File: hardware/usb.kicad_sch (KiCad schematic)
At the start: 2 parts

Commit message: Add the Cube project
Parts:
- added C?: 100n, Capacitor_SMD:C_0402_1005Metric_Pad0.74x0.62mm_HandSolder, symbol Device:C_Small
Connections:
- net +5V: now also C?.1
- net GND: now also C?.2
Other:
- note removed: "Place close to the connector"
- moved on the sheet: J?, U?

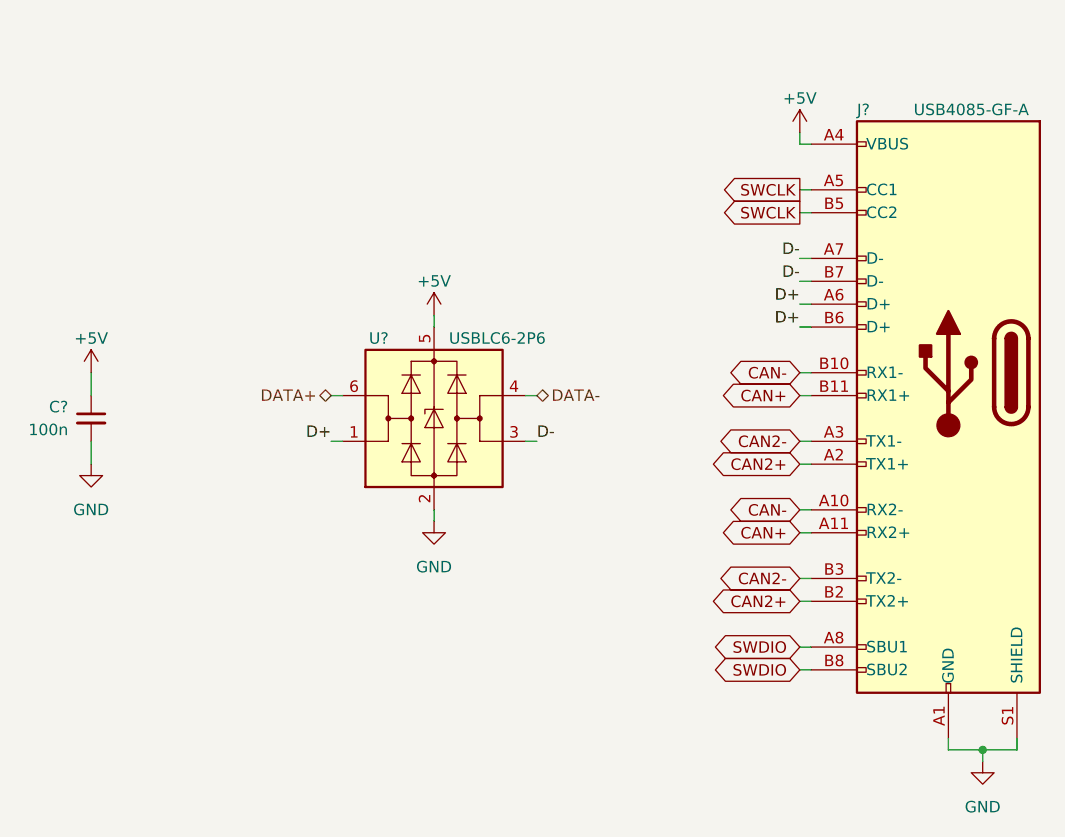
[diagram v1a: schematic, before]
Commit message: Improve the schematic
- add anti-aliasing filters
- rearrange the main connector signals
- improve the power filtering
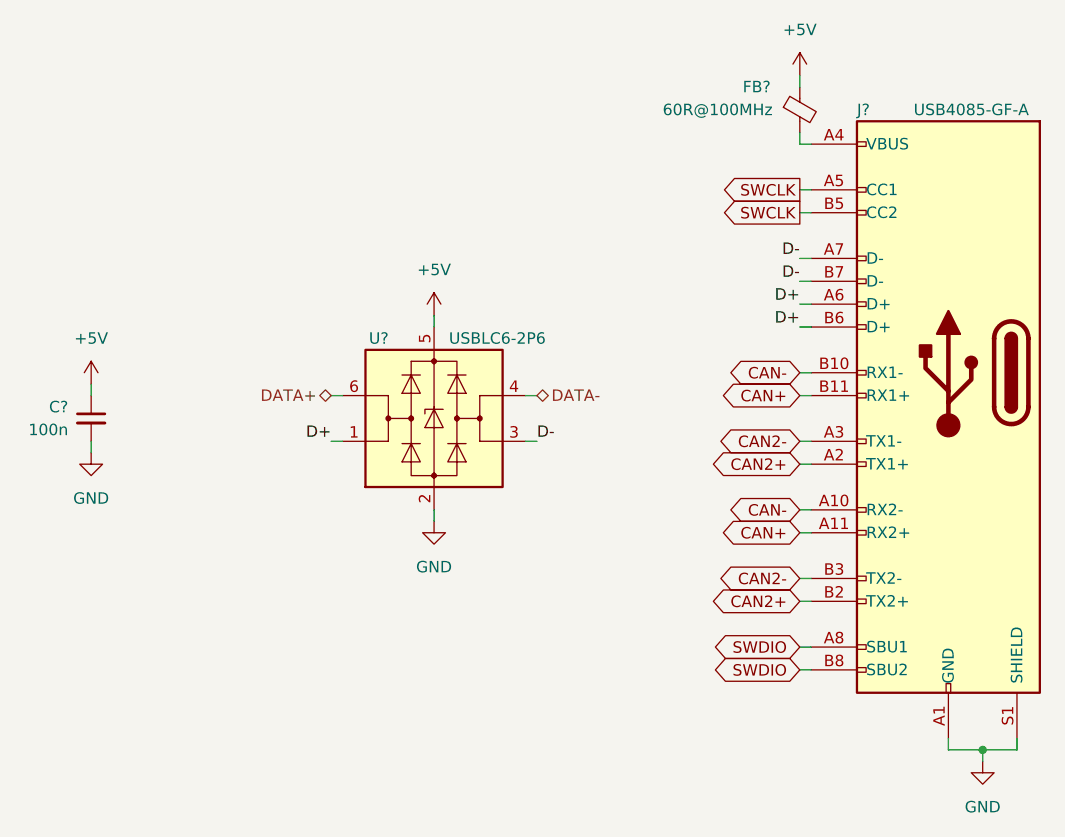
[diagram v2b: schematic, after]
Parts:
- added FB?: 60R@100MHz, Inductor_SMD:L_0603_1608Metric, symbol Device:FerriteBead_Small
- C?: footprint Capacitor_SMD:C_0402_1005Metric_Pad0.74x0.62mm_HandSolder -> Capacitor_SMD:C_0603_1608Metric
- J?: footprint Frontbox:CUI_UJ31-CH-31-SMT-TR -> Local_Library:CUI_UJ31-CH-31-SMT-TR
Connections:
- net +5V: now also FB?.1; no longer J?.A4 (VBUS), J?.A9 (VBUS), J?.B4 (VBUS), J?.B9 (VBUS)
- new net: FB?.2, J?.A4 (VBUS), J?.A9 (VBUS), J?.B4 (VBUS), J?.B9 (VBUS)
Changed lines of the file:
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@@
     (stroke (width 0) (type default))
   )
-  (wire (pts (xy 101.6 101.6) (xy 101.6 104.14))
+  (wire (pts (xy 101.6 101.6) (xy 101.6 102.87))
     (stroke (width 0) (type default))
   )
@@
     (stroke (width 0) (type default))
   )
-  (wire (pts (xy 101.6 93.98) (xy 101.6 96.52))
+  (wire (pts (xy 101.6 95.25) (xy 101.6 96.52))
+    (stroke (width 0) (type default))
+  )
+  (wire (pts (xy 180.34 60.96) (xy 180.34 62.23))
     (stroke (width 0) (type default))
   )
@@
     (effects (font (size 1.27 1.27)) (justify left))
   )
-  (symbol (lib_id "power:GND") (at 101.6 104.14 0) (unit 1)
-    (in_bom yes) (on_board yes) (dnp no)
-    (property "Reference" "#PWR?" (at 101.6 110.49 0)
-      (effects (font (size 1.27 1.27)) hide)
-    )
-    (property "Value" "GND" (at 101.6 109.22 0)
-      (effects (font (size 1.27 1.27)))
-    )
-    (property "Footprint" "" (at 101.6 104.14 0)
-      (effects (font (size 1.27 1.27)) hide)
-    )
-    (property "Datasheet" "" (at 101.6 104.14 0)
-      (effects (font (size 1.27 1.27)) hide)
-    )
-    (pin "1")
-    (instances
-      (project "rearbox"
-        (path "/b652b05a-4e3d-4ad1-b032-18886abe7d45"
-          (reference "#PWR?") (unit 1)
-        )
-        (path "/b652b05a-4e3d-4ad1-b032-18886abe7d45/1a71c66a-e6f2-4e7d-92f3-10826884049d"
-          (reference "#PWR0107") (unit 1)
-        )
-      )
-    )
-  )
-  (symbol (lib_id "power:+5V") (at 180.34 67.31 0) (mirror y) (unit 1)
-    (in_bom yes) (on_board yes) (dnp no) (fields_autoplaced)
-    (property "Reference" "#PWR?" (at 180.34 71.12 0)
-      (effects (font (size 1.27 1.27)) hide)
-    )
-    (property "Value" "+5V" (at 180.34 63.5 0)
-      (effects (font (size 1.27 1.27)))
-    )
-    (property "Footprint" "" (at 180.34 67.31 0)
-      (effects (font (size 1.27 1.27)) hide)
-    )
-    (property "Datasheet" "" (at 180.34 67.31 0)
+  (symbol (lib_id "power:GND") (at 101.6 102.87 0) (unit 1)
+    (in_bom yes) (on_board yes) (dnp no)
+    (property "Reference" "#PWR?" (at 101.6 109.22 0)
+      (effects (font (size 1.27 1.27)) hide)
+    )
+    (property "Value" "GND" (at 101.6 107.95 0)
+      (effects (font (size 1.27 1.27)))
+    )
+    (property "Footprint" "" (at 101.6 102.87 0)
+      (effects (font (size 1.27 1.27)) hide)
+    )
+    (property "Datasheet" "" (at 101.6 102.87 0)
+      (effects (font (size 1.27 1.27)) hide)
+    )
+    (pin "1")
+    (instances
+      (project "rearbox"
+        (path "/b652b05a-4e3d-4ad1-b032-18886abe7d45"
+          (reference "#PWR?") (unit 1)
+        )
+        (path "/b652b05a-4e3d-4ad1-b032-18886abe7d45/1a71c66a-e6f2-4e7d-92f3-10826884049d"
+          (reference "#PWR0121") (unit 1)
+        )
+      )
+    )
+  )
+  (symbol (lib_id "power:+5V") (at 180.34 60.96 0) (mirror y) (unit 1)
+    (in_bom yes) (on_board yes) (dnp no)
+    (property "Reference" "#PWR?" (at 180.34 64.77 0)
+      (effects (font (size 1.27 1.27)) hide)
+    )
+    (property "Value" "+5V" (at 180.34 55.88 0)
+      (effects (font (size 1.27 1.27)))
+    )
+    (property "Footprint" "" (at 180.34 60.96 0)
+      (effects (font (size 1.27 1.27)) hide)
+    )
+    (property "Datasheet" "" (at 180.34 60.96 0)
       (effects (font (size 1.27 1.27)) hide)
     )
@@
         )
         (path "/b652b05a-4e3d-4ad1-b032-18886abe7d45/1a71c66a-e6f2-4e7d-92f3-10826884049d"
-          (reference "#PWR0110") (unit 1)
+          (reference "#PWR0124") (unit 1)
+        )
+      )
+    )
+  )
+  (symbol (lib_id "Device:FerriteBead_Small") (at 180.34 64.77 0) (unit 1)
+    (in_bom yes) (on_board yes) (dnp no)
+    (property "Reference" "FB?" (at 173.99 62.23 0)
+      (effects (font (size 1.27 1.27)) (justify left))
+    )
+    (property "Value" "60R@100MHz" (at 165.1 64.77 0)
+      (effects (font (size 1.27 1.27)) (justify left))
+    )
+    (property "Footprint" "Inductor_SMD:L_0603_1608Metric" (at 178.562 64.77 90)
+      (effects (font (size 1.27 1.27)) hide)
+    )
+    (property "Datasheet" "~" (at 180.34 64.77 0)
+      (effects (font (size 1.27 1.27)) hide)
+    )
+    (pin "1")
+    (pin "2")
+    (instances
+      (project "rearbox"
+        (path "/b652b05a-4e3d-4ad1-b032-18886abe7d45/38408e41-dfb1-4c27-acb0-3f1224cc8789"
+          (reference "FB?") (unit 1)
+        )
+        (path "/b652b05a-4e3d-4ad1-b032-18886abe7d45/38408e41-dfb1-4c27-acb0-3f1224cc8789/eec2c93a-0fce-4d3a-ab43-9e1e0481c06c"
+          (reference "FB3") (unit 1)
+        )
+        (path "/b652b05a-4e3d-4ad1-b032-18886abe7d45/38408e41-dfb1-4c27-acb0-3f1224cc8789/f1ed15a3-9302-436f-b25a-713477aeadf3"
+          (reference "FB1") (unit 1)
+        )
+        (path "/b652b05a-4e3d-4ad1-b032-18886abe7d45/1a71c66a-e6f2-4e7d-92f3-10826884049d"
+          (reference "FB7") (unit 1)
         )
       )
@@
         )
         (path "/b652b05a-4e3d-4ad1-b032-18886abe7d45/1a71c66a-e6f2-4e7d-92f3-10826884049d"
-          (reference "U12") (unit 1)
-        )
-      )
-    )
-  )
-  (symbol (lib_id "power:+5V") (at 101.6 93.98 0) (unit 1)
-    (in_bom yes) (on_board yes) (dnp no) (fields_autoplaced)
-    (property "Reference" "#PWR?" (at 101.6 97.79 0)
+          (reference "U13") (unit 1)
+        )
+      )
+    )
+  )
+  (symbol (lib_id "power:+5V") (at 101.6 95.25 0) (unit 1)
+    (in_bom yes) (on_board yes) (dnp no)
+    (property "Reference" "#PWR?" (at 101.6 99.06 0)
       (effects (font (size 1.27 1.27)) hide)
     )
@@
       (effects (font (size 1.27 1.27)))
     )
-    (property "Footprint" "" (at 101.6 93.98 0)
-      (effects (font (size 1.27 1.27)) hide)
-    )
-    (property "Datasheet" "" (at 101.6 93.98 0)
-      (effects (font (size 1.27 1.27)) hide)
-    )
-    (pin "1")
-    (instances
-      (project "rearbox"
-        (path "/b652b05a-4e3d-4ad1-b032-18886abe7d45"
-          (reference "#PWR?") (unit 1)
-        )
-        (path "/b652b05a-4e3d-4ad1-b032-18886abe7d45/1a71c66a-e6f2-4e7d-92f3-10826884049d"
-          (reference "#PWR0106") (unit 1)
+    (property "Footprint" "" (at 101.6 95.25 0)
+      (effects (font (size 1.27 1.27)) hide)
+    )
+    (property "Datasheet" "" (at 101.6 95.25 0)
+      (effects (font (size 1.27 1.27)) hide)
+    )
+    (pin "1")
+    (instances
+      (project "rearbox"
+        (path "/b652b05a-4e3d-4ad1-b032-18886abe7d45"
+          (reference "#PWR?") (unit 1)
+        )
+        (path "/b652b05a-4e3d-4ad1-b032-18886abe7d45/1a71c66a-e6f2-4e7d-92f3-10826884049d"
+          (reference "#PWR0120") (unit 1)
         )
       )
@@
         )
         (path "/b652b05a-4e3d-4ad1-b032-18886abe7d45/1a71c66a-e6f2-4e7d-92f3-10826884049d"
-          (reference "#PWR0109") (unit 1)
+          (reference "#PWR0123") (unit 1)
         )
       )
@@
       (effects (font (size 1.27 1.27)))
     )
-    (property "Footprint" "Frontbox:CUI_UJ31-CH-31-SMT-TR" (at 193.04 93.98 0)
+    (property "Footprint" "Local_Library:CUI_UJ31-CH-31-SMT-TR" (at 193.04 93.98 0)
       (effects (font (size 1.27 1.27)) hide)
     )
@@
   )
   (symbol (lib_id "power:+5V") (at 139.7 87.63 0) (unit 1)
-    (in_bom yes) (on_board yes) (dnp no) (fields_autoplaced)
+    (in_bom yes) (on_board yes) (dnp no)
     (property "Reference" "#PWR?" (at 139.7 91.44 0)
       (effects (font (size 1.27 1.27)) hide)
     )
-    (property "Value" "+5V" (at 139.7 83.82 0)
+    (property "Value" "+5V" (at 139.7 82.55 0)
       (effects (font (size 1.27 1.27)))
     )
@@
         )
         (path "/b652b05a-4e3d-4ad1-b032-18886abe7d45/1a71c66a-e6f2-4e7d-92f3-10826884049d"
-          (reference "#PWR0108") (unit 1)
+          (reference "#PWR0122") (unit 1)
         )
       )
@@
         )
         (path "/b652b05a-4e3d-4ad1-b032-18886abe7d45/1a71c66a-e6f2-4e7d-92f3-10826884049d"
-          (reference "#PWR0111") (unit 1)
+          (reference "#PWR0125") (unit 1)
         )
       )
@@
       (effects (font (size 1.27 1.27)) (justify left))
     )
-    (property "Footprint" "Capacitor_SMD:C_0402_1005Metric_Pad0.74x0.62mm_HandSolder" (at 101.6 99.06 0)
+    (property "Footprint" "Capacitor_SMD:C_0603_1608Metric" (at 101.6 99.06 0)
       (effects (font (size 1.27 1.27)) hide)
     )
@@
         )
         (path "/b652b05a-4e3d-4ad1-b032-18886abe7d45/1a71c66a-e6f2-4e7d-92f3-10826884049d"
-          (reference "C29") (unit 1)
-        )
-      )
+          (reference "C35") (unit 1)
+        )
+      )

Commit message: Set component values
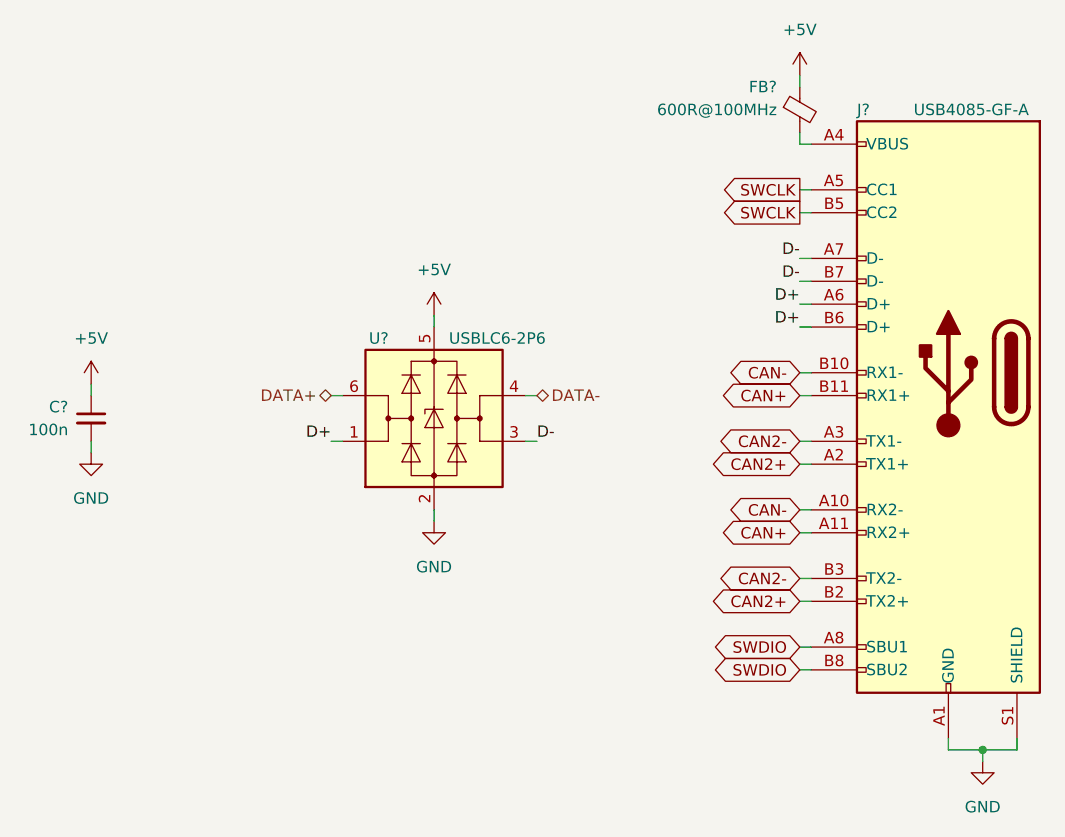
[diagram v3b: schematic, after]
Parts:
- FB?: value 60R@100MHz -> 600R@100MHz
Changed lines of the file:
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@@
+    (stroke (width 0) (type default))
+  )
+  (wire (pts (xy 180.34 119.38) (xy 181.61 119.38))
+    (stroke (width 0) (type default))
+  )
+  (wire (pts (xy 139.7 87.63) (xy 139.7 88.9))
+    (stroke (width 0) (type default))
+  )
+  (wire (pts (xy 180.34 83.82) (xy 181.61 83.82))
+    (stroke (width 0) (type default))
+  )
+  (wire (pts (xy 151.13 101.6) (xy 149.86 101.6))
+    (stroke (width 0) (type default))
+  )
+  (wire (pts (xy 180.34 101.6) (xy 181.61 101.6))
+    (stroke (width 0) (type default))
+  )
+  (wire (pts (xy 180.34 111.76) (xy 181.61 111.76))
+    (stroke (width 0) (type default))
+  )
+  (wire (pts (xy 180.34 73.66) (xy 181.61 73.66))
+    (stroke (width 0) (type default))
+  )
+  (wire (pts (xy 180.34 76.2) (xy 181.61 76.2))
+    (stroke (width 0) (type default))
+  )
+  (wire (pts (xy 181.61 68.58) (xy 180.34 68.58))
+    (stroke (width 0) (type default))
+  )
+  (wire (pts (xy 180.34 109.22) (xy 181.61 109.22))
+    (stroke (width 0) (type default))
+  )
+  (wire (pts (xy 180.34 68.58) (xy 180.34 67.31))
+    (stroke (width 0) (type default))
+  )
+  (wire (pts (xy 204.47 134.62) (xy 204.47 135.89))
+    (stroke (width 0) (type default))
+  )
+  (wire (pts (xy 180.34 104.14) (xy 181.61 104.14))
+    (stroke (width 0) (type default))
+  )
+  (wire (pts (xy 101.6 101.6) (xy 101.6 102.87))
+    (stroke (width 0) (type default))
+  )
+  (wire (pts (xy 128.27 101.6) (xy 129.54 101.6))
+    (stroke (width 0) (type default))
+  )
+  (wire (pts (xy 180.34 86.36) (xy 181.61 86.36))
+    (stroke (width 0) (type default))
+  )
+  (wire (pts (xy 180.34 93.98) (xy 181.61 93.98))
+    (stroke (width 0) (type default))
+  )
+  (wire (pts (xy 200.66 135.89) (xy 196.85 135.89))
+    (stroke (width 0) (type default))
+  )
+  (wire (pts (xy 180.34 96.52) (xy 181.61 96.52))
+    (stroke (width 0) (type default))
+  )
+  (wire (pts (xy 200.66 135.89) (xy 200.66 137.16))
+    (stroke (width 0) (type default))
+  )
+  (wire (pts (xy 180.34 81.28) (xy 181.61 81.28))
+    (stroke (width 0) (type default))
+  )
+  (wire (pts (xy 180.34 88.9) (xy 181.61 88.9))
     (stroke (width 0) (type default))
   )
@@
     (stroke (width 0) (type default))
   )
-  (wire (pts (xy 180.34 119.38) (xy 181.61 119.38))
-    (stroke (width 0) (type default))
-  )
-  (wire (pts (xy 139.7 87.63) (xy 139.7 88.9))
-    (stroke (width 0) (type default))
-  )
-  (wire (pts (xy 180.34 83.82) (xy 181.61 83.82))
-    (stroke (width 0) (type default))
-  )
-  (wire (pts (xy 151.13 101.6) (xy 149.86 101.6))
+  (wire (pts (xy 101.6 95.25) (xy 101.6 96.52))
     (stroke (width 0) (type default))
   )
@@
     (stroke (width 0) (type default))
   )
-  (wire (pts (xy 180.34 101.6) (xy 181.61 101.6))
-    (stroke (width 0) (type default))
-  )
-  (wire (pts (xy 180.34 111.76) (xy 181.61 111.76))
-    (stroke (width 0) (type default))
-  )
-  (wire (pts (xy 180.34 73.66) (xy 181.61 73.66))
-    (stroke (width 0) (type default))
-  )
-  (wire (pts (xy 180.34 76.2) (xy 181.61 76.2))
-    (stroke (width 0) (type default))
-  )
-  (wire (pts (xy 181.61 68.58) (xy 180.34 68.58))
-    (stroke (width 0) (type default))
-  )
-  (wire (pts (xy 180.34 109.22) (xy 181.61 109.22))
-    (stroke (width 0) (type default))
-  )
-  (wire (pts (xy 180.34 68.58) (xy 180.34 67.31))
-    (stroke (width 0) (type default))
-  )
-  (wire (pts (xy 204.47 134.62) (xy 204.47 135.89))
-    (stroke (width 0) (type default))
-  )
-  (wire (pts (xy 180.34 104.14) (xy 181.61 104.14))
-    (stroke (width 0) (type default))
-  )
-  (wire (pts (xy 101.6 101.6) (xy 101.6 102.87))
-    (stroke (width 0) (type default))
-  )
-  (wire (pts (xy 128.27 101.6) (xy 129.54 101.6))
-    (stroke (width 0) (type default))
-  )
-  (wire (pts (xy 180.34 86.36) (xy 181.61 86.36))
-    (stroke (width 0) (type default))
-  )
-  (wire (pts (xy 180.34 93.98) (xy 181.61 93.98))
-    (stroke (width 0) (type default))
-  )
-  (wire (pts (xy 180.34 96.52) (xy 181.61 96.52))
-    (stroke (width 0) (type default))
-  )
-  (wire (pts (xy 180.34 81.28) (xy 181.61 81.28))
-    (stroke (width 0) (type default))
-  )
-  (wire (pts (xy 180.34 88.9) (xy 181.61 88.9))
-    (stroke (width 0) (type default))
-  )
-  (wire (pts (xy 200.66 137.16) (xy 200.66 135.89))
-    (stroke (width 0) (type default))
-  )
-  (wire (pts (xy 101.6 95.25) (xy 101.6 96.52))
-    (stroke (width 0) (type default))
-  )
   (wire (pts (xy 180.34 60.96) (xy 180.34 62.23))
-    (stroke (width 0) (type default))
-  )
-  (wire (pts (xy 200.66 135.89) (xy 196.85 135.89))
     (stroke (width 0) (type default))
   )
@@
   (symbol (lib_id "Device:FerriteBead_Small") (at 180.34 64.77 0) (unit 1)
     (in_bom yes) (on_board yes) (dnp no)
-    (property "Reference" "FB?" (at 173.99 62.23 0)
-      (effects (font (size 1.27 1.27)) (justify left))
-    )
-    (property "Value" "60R@100MHz" (at 165.1 64.77 0)
-      (effects (font (size 1.27 1.27)) (justify left))
+    (property "Reference" "FB?" (at 177.8 62.23 0)
+      (effects (font (size 1.27 1.27)) (justify right))
+    )
+    (property "Value" "600R@100MHz" (at 177.8 64.77 0)
+      (effects (font (size 1.27 1.27)) (justify right))
     )
     (property "Footprint" "Inductor_SMD:L_0603_1608Metric" (at 178.562 64.77 90)
@@
         (path "/b652b05a-4e3d-4ad1-b032-18886abe7d45/1a71c66a-e6f2-4e7d-92f3-10826884049d"
           (reference "#PWR0120") (unit 1)
+        )
+      )
+    )
+  )
+  (symbol (lib_id "power:GND") (at 200.66 137.16 0) (unit 1)
+    (in_bom yes) (on_board yes) (dnp no) (fields_autoplaced)
+    (property "Reference" "#PWR0125" (at 200.66 143.51 0)
+      (effects (font (size 1.27 1.27)) hide)
+    )
+    (property "Value" "GND" (at 200.66 142.24 0)
+      (effects (font (size 1.27 1.27)))
+    )
+    (property "Footprint" "" (at 200.66 137.16 0)
+      (effects (font (size 1.27 1.27)) hide)
+    )
+    (property "Datasheet" "" (at 200.66 137.16 0)
+      (effects (font (size 1.27 1.27)) hide)
+    )
+    (pin "1")
+    (instances
+      (project "rearbox"
+        (path "/b652b05a-4e3d-4ad1-b032-18886abe7d45/1a71c66a-e6f2-4e7d-92f3-10826884049d"
+          (reference "#PWR0125") (unit 1)
         )
       )
@@
     )
   )
-  (symbol (lib_id "power:GND") (at 200.66 137.16 0) (mirror y) (unit 1)
-    (in_bom yes) (on_board yes) (dnp no)
-    (property "Reference" "#PWR?" (at 200.66 143.51 0)
-      (effects (font (size 1.27 1.27)) hide)
-    )
-    (property "Value" "GND" (at 200.66 142.24 0)
-      (effects (font (size 1.27 1.27)))
-    )
-    (property "Footprint" "" (at 200.66 137.16 0)
-      (effects (font (size 1.27 1.27)) hide)
-    )
-    (property "Datasheet" "" (at 200.66 137.16 0)
-      (effects (font (size 1.27 1.27)) hide)
-    )
-    (pin "1")
-    (instances
-      (project "rearbox"
-        (path "/b652b05a-4e3d-4ad1-b032-18886abe7d45"
-          (reference "#PWR?") (unit 1)
-        )
-        (path "/b652b05a-4e3d-4ad1-b032-18886abe7d45/cf65c657-8245-46fb-8929-d241bd579513"
-          (reference "#PWR?") (unit 1)
-        )
-        (path "/b652b05a-4e3d-4ad1-b032-18886abe7d45/1a71c66a-e6f2-4e7d-92f3-10826884049d"
-          (reference "#PWR0125") (unit 1)
-        )
-      )
-    )
-  )
   (symbol (lib_id "Device:C_Small") (at 101.6 99.06 0) (mirror y) (unit 1)
     (in_bom yes) (on_board yes) (dnp no)
@@
         )
         (path "/b652b05a-4e3d-4ad1-b032-18886abe7d45/1a71c66a-e6f2-4e7d-92f3-10826884049d"
-          (reference "C35") (unit 1)
-        )
-      )
+          (reference "C36") (unit 1)
+        )
+      )
